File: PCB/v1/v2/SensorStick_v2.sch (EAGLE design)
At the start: 62 parts, among them IC1 STM32L412RBT6, J1 DST310S_32.768KHZ, J2 10118192-0001LF, U1 BMI088, U2 LD39050PU33R, Y1 8MHz

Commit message: Jesus - More merge changes
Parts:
- removed C2, C37: 4.7p, GQM2195C2E4R7BB12D(4_7p):GQM2195C2E4R7BB12D
- removed C3, C35: 20p, CC0402KPX7R7BB104(0402cap_foot):CC0402KPX7R7BB104
- removed J1: DST310S_32.768KHZ, ce-capstone-2022:DST310S_32.768KHZ_DST310S_32.768KHZ
- removed R4: 220, RC0805FR-10220RL:RC0805FR-10220RL
- removed Y1: 8MHz, ce-capstone:ABLS-8.000MHZ-B2-T
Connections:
- removed net N$3: C3.1, R4.2, Y1.1
- removed net PC14-OSC32-IN: C37.1, J1.1
- removed net PC15-OSC32-OUT: C2.1, J1.2
- removed net PH0-OSC-IN: C35.1, Y1.2
- removed net PH1-OSC-OUT: R4.1
- net GND: no longer C2.2, C3.2, C35.2, C37.2
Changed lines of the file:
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@@
 <part name="FB1" library="ce-capstone" deviceset="BK1608HS601-T" device=""/>
 <part name="GND4" library="supply1" library_urn="urn:adsk.eagle:library:371" deviceset="GND" device=""/>
-<part name="Y1" library="ce-capstone" deviceset="ABLS-8.000MHZ-B2-T" device="" value="8MHz"/>
-<part name="GND5" library="supply1" library_urn="urn:adsk.eagle:library:371" deviceset="GND" device=""/>
-<part name="GND6" library="supply1" library_urn="urn:adsk.eagle:library:371" deviceset="GND" device=""/>
 <part name="GND7" library="supply1" library_urn="urn:adsk.eagle:library:371" deviceset="GND" device=""/>
 <part name="J2" library="ce-capstone" deviceset="10118192-0001LF" device=""/>
@@
 <part name="C33" library="GRT31C5C2A104JA12L(0_1u)" deviceset="GRT31C5C2A104JA12L" device="" value="100n"/>
 <part name="C34" library="GRT31C5C2A104JA12L(0_1u)" deviceset="GRT31C5C2A104JA12L" device="" value="100n"/>
-<part name="C37" library="GQM2195C2E4R7BB12D(4_7p)" deviceset="GQM2195C2E4R7BB12D" device="" value="4.7p"/>
 <part name="C39" library="GRT21BC71H475KE13L(4_7u)" deviceset="GRT21BC71H475KE13L" device="" value="4.7u"/>
 <part name="C40" library="GRM31CR73A103KW03L(0_01u)" deviceset="GRM31CR73A103KW03L" device="" value="10n"/>
-<part name="C2" library="GQM2195C2E4R7BB12D(4_7p)" deviceset="GQM2195C2E4R7BB12D" device="" value="4.7p"/>
 <part name="C4" library="GRM219R61H105KA73D(1u)" deviceset="GRM219R61H105KA73D" device="" value="1u"/>
-<part name="R4" library="RC0805FR-10220RL" deviceset="RC0805FR-10220RL" device="" value="220"/>
 <part name="R6" library="RC0805FR-131KL" deviceset="RC0805FR-131KL" device="" value="1K"/>
 <part name="R7" library="RC0805FR-131KL" deviceset="RC0805FR-131KL" device="" value="1K"/>
@@
 <part name="JP3" library="pinhead" library_urn="urn:adsk.eagle:library:325" deviceset="PINHD-2X4" device="" package3d_urn="urn:adsk.eagle:package:22461/2"/>
 <part name="JP8" library="pinhead" library_urn="urn:adsk.eagle:library:325" deviceset="PINHD-2X4" device="" package3d_urn="urn:adsk.eagle:package:22461/2"/>
-<part name="J1" library="ce-capstone-2022" deviceset="DST310S_32.768KHZ_DST310S_32.768KHZ" device="" value="DST310S_32.768KHZ"/>
 <part name="S1" library="ce-capstone-2022" deviceset="SWITCH-TACT_DTSM-6" device=""/>
 <part name="D1" library="ce-capstone-2022" deviceset="1N5819HW-7-F_1N5819HW-7-F" device=""/>
-<part name="C35" library="CC0402KPX7R7BB104(0402cap_foot)" deviceset="CC0402KPX7R7BB104" device="" value="20p"/>
-<part name="C3" library="CC0402KPX7R7BB104(0402cap_foot)" deviceset="CC0402KPX7R7BB104" device="" value="20p"/>
 <part name="U1" library="BMI088" deviceset="BMI088" device=""/>
 <part name="FRAME2" library="frames" library_urn="urn:adsk.eagle:library:229" deviceset="FRAME_C_L" device=""/>
@@
 <attribute name="VALUE" x="-96.52" y="99.06" size="1.778" layer="96"/>
 </instance>
-<instance part="Y1" gate="G$1" x="7.62" y="208.28" smashed="yes" rot="R90">
-<attribute name="NAME" x="5.333490625" y="203.19886875" size="1.7784" layer="95" rot="R90"/>
-<attribute name="VALUE" x="11.43073125" y="202.69093125" size="1.778340625" layer="96" rot="R90"/>
-</instance>
-<instance part="GND5" gate="1" x="50.8" y="198.12" smashed="yes">
-<attribute name="VALUE" x="48.26" y="195.58" size="1.778" layer="96"/>
-</instance>
-<instance part="GND6" gate="1" x="50.8" y="167.64" smashed="yes">
-<attribute name="VALUE" x="48.26" y="165.1" size="1.778" layer="96"/>
-</instance>
 <instance part="GND7" gate="1" x="299.72" y="144.78" smashed="yes">
 <attribute name="VALUE" x="297.18" y="139.7" size="1.778" layer="96"/>
@@
 <attribute name="VALUE" x="-110.49" y="143.51" size="1.778" layer="96" align="center-left"/>
 </instance>
-<instance part="C37" gate="G$1" x="22.86" y="185.42" smashed="yes">
-<attribute name="NAME" x="31.75" y="191.77" size="1.778" layer="95" align="center-left"/>
-<attribute name="VALUE" x="31.75" y="189.23" size="1.778" layer="96" align="center-left"/>
-</instance>
 <instance part="C39" gate="G$1" x="-124.46" y="223.52" smashed="yes">
 <attribute name="NAME" x="-115.57" y="229.87" size="1.778" layer="95" align="center-left"/>
@@
 <attribute name="VALUE" x="-110.49" y="113.03" size="1.778" layer="96" align="center-left"/>
 </instance>
-<instance part="C2" gate="G$1" x="22.86" y="170.18" smashed="yes">
-<attribute name="NAME" x="31.75" y="176.53" size="1.778" layer="95" align="center-left"/>
-<attribute name="VALUE" x="31.75" y="173.99" size="1.778" layer="96" align="center-left"/>
-</instance>
 <instance part="C4" gate="G$1" x="271.78" y="223.52" smashed="yes" rot="R90">
 <attribute name="NAME" x="265.43" y="232.41" size="1.778" layer="95" rot="R90" align="center-left"/>
 <attribute name="VALUE" x="267.97" y="232.41" size="1.778" layer="96" rot="R90" align="center-left"/>
 </instance>
-<instance part="R4" gate="G$1" x="-30.48" y="200.66" smashed="yes">
-<attribute name="NAME" x="-16.51" y="207.01" size="1.778" layer="95" align="center-left"/>
-<attribute name="VALUE" x="-16.51" y="204.47" size="1.778" layer="96" align="center-left"/>
-</instance>
 <instance part="R6" gate="G$1" x="299.72" y="218.44" smashed="yes" rot="R90">
 <attribute name="NAME" x="293.37" y="232.41" size="1.778" layer="95" rot="R90" align="center-left"/>
@@
 <attribute name="VALUE" x="-133.35" y="45.72" size="1.778" layer="96"/>
 </instance>
-<instance part="J1" gate="G$1" x="-2.54" y="177.8" smashed="yes">
-<attribute name="NAME" x="13.97" y="180.34" size="1.778" layer="95" align="center-left"/>
-<attribute name="VALUE" x="1.27" y="182.88" size="1.778" layer="96" align="center-left"/>
-</instance>
 <instance part="S1" gate="G$1" x="302.26" y="167.64" smashed="yes" rot="R180">
 <attribute name="NAME" x="308.61" y="170.18" size="1.778" layer="95" rot="R270"/>
@@
 <attribute name="NAME" x="173.99" y="231.14" size="1.778" layer="95" rot="R180" align="center-left"/>
 <attribute name="VALUE" x="189.23" y="241.3" size="1.778" layer="96" rot="R180" align="center-left"/>
-</instance>
-<instance part="C35" gate="G$1" x="25.4" y="215.9" smashed="yes">
-<attribute name="NAME" x="31.75" y="224.79" size="1.778" layer="95" align="center-left"/>
-<attribute name="VALUE" x="31.75" y="222.25" size="1.778" layer="96" align="center-left"/>
-</instance>
-<instance part="C3" gate="G$1" x="25.4" y="200.66" smashed="yes">
-<attribute name="NAME" x="34.29" y="207.01" size="1.778" layer="95" align="center-left"/>
-<attribute name="VALUE" x="34.29" y="204.47" size="1.778" layer="96" align="center-left"/>
 </instance>
 <instance part="U1" gate="A" x="-30.48" y="96.52" smashed="yes">
@@
 </segment>
 <segment>
-<pinref part="GND5" gate="1" pin="GND"/>
-<wire x1="50.8" y1="215.9" x2="50.8" y2="200.66" width="0.1524" layer="91"/>
-<wire x1="38.1" y1="200.66" x2="50.8" y2="200.66" width="0.1524" layer="91"/>
-<junction x="50.8" y="200.66"/>
-<wire x1="38.1" y1="215.9" x2="50.8" y2="215.9" width="0.1524" layer="91"/>
-<pinref part="C35" gate="G$1" pin="2"/>
-<pinref part="C3" gate="G$1" pin="2"/>
-</segment>
-<segment>
-<pinref part="GND6" gate="1" pin="GND"/>
-<wire x1="50.8" y1="185.42" x2="50.8" y2="170.18" width="0.1524" layer="91"/>
-<pinref part="C2" gate="G$1" pin="2"/>
-<wire x1="35.56" y1="170.18" x2="50.8" y2="170.18" width="0.1524" layer="91"/>
-<junction x="50.8" y="170.18"/>
-<pinref part="C37" gate="G$1" pin="2"/>
-<wire x1="35.56" y1="185.42" x2="50.8" y2="185.42" width="0.1524" layer="91"/>
-</segment>
-<segment>
 <wire x1="276.86" y1="157.48" x2="299.72" y2="157.48" width="0.1524" layer="91"/>
 <wire x1="299.72" y1="157.48" x2="302.26" y2="157.48" width="0.1524" layer="91"/>
@@
 </segment>
 </net>
-<net name="PH1-OSC-OUT" class="0">
-<segment>
-<wire x1="-30.48" y1="200.66" x2="-50.8" y2="200.66" width="0.1524" layer="91"/>
-<label x="-45.72" y="200.66" size="1.778" layer="95"/>
-<pinref part="R4" gate="G$1" pin="1"/>
-</segment>
-</net>
-<net name="PH0-OSC-IN" class="0">
-<segment>
-<pinref part="Y1" gate="G$1" pin="2"/>
-<wire x1="7.62" y1="213.36" x2="7.62" y2="215.9" width="0.1524" layer="91"/>
-<wire x1="7.62" y1="215.9" x2="-40.64" y2="215.9" width="0.1524" layer="91"/>
-<label x="-40.64" y="215.9" size="1.778" layer="95"/>
-<wire x1="7.62" y1="215.9" x2="25.4" y2="215.9" width="0.1524" layer="91"/>
-<junction x="7.62" y="215.9"/>
-<pinref part="C35" gate="G$1" pin="1"/>
-</segment>
-</net>
-<net name="PC15-OSC32-OUT" class="0">
-<segment>
-<wire x1="22.86" y1="170.18" x2="-2.54" y2="170.18" width="0.1524" layer="91"/>
-<label x="-45.72" y="170.18" size="1.778" layer="95"/>
-<pinref part="C2" gate="G$1" pin="1"/>
-<pinref part="J1" gate="G$1" pin="2"/>
-<wire x1="-2.54" y1="170.18" x2="-48.26" y2="170.18" width="0.1524" layer="91"/>
-<wire x1="-2.54" y1="175.26" x2="-2.54" y2="170.18" width="0.1524" layer="91"/>
-<junction x="-2.54" y="170.18"/>
-</segment>
-</net>
-<net name="PC14-OSC32-IN" class="0">
-<segment>
-<wire x1="22.86" y1="185.42" x2="-2.54" y2="185.42" width="0.1524" layer="91"/>
-<label x="-45.72" y="185.42" size="1.778" layer="95"/>
-<pinref part="C37" gate="G$1" pin="1"/>
-<pinref part="J1" gate="G$1" pin="1"/>
-<wire x1="-2.54" y1="185.42" x2="-48.26" y2="185.42" width="0.1524" layer="91"/>
-<wire x1="-2.54" y1="177.8" x2="-2.54" y2="185.42" width="0.1524" layer="91"/>
-<junction x="-2.54" y="185.42"/>
-</segment>
-</net>
 <net name="5V_IN" class="0">
 <segment>
@@
 </segment>
 </net>
-<net name="N$3" class="0">
-<segment>
-<pinref part="Y1" gate="G$1" pin="1"/>
-<wire x1="-12.7" y1="200.66" x2="7.62" y2="200.66" width="0.1524" layer="91"/>
-<wire x1="7.62" y1="203.2" x2="7.62" y2="200.66" width="0.1524" layer="91"/>
-<wire x1="7.62" y1="200.66" x2="25.4" y2="200.66" width="0.1524" layer="91"/>
-<junction x="7.62" y="200.66"/>
-<pinref part="R4" gate="G$1" pin="2"/>
-<pinref part="C3" gate="G$1" pin="1"/>
-</segment>
-</net>

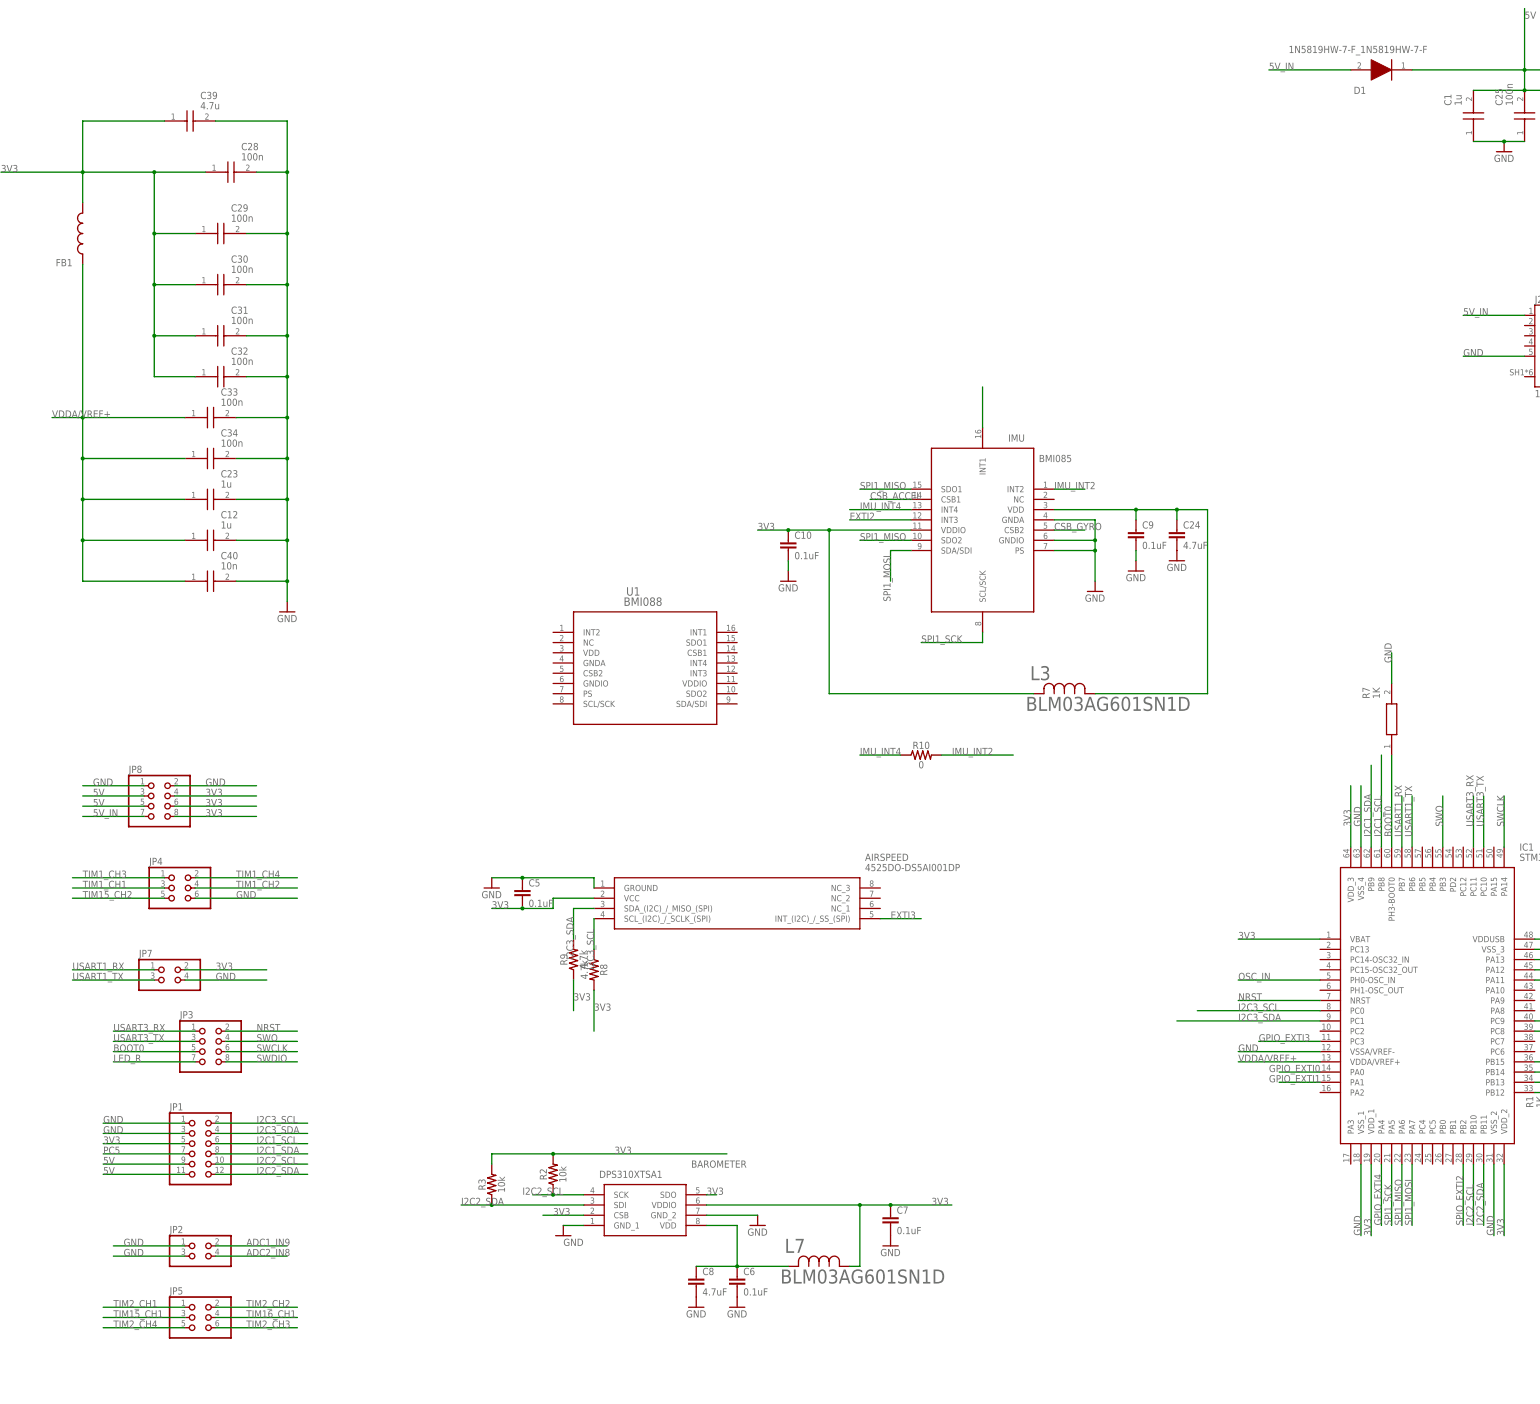
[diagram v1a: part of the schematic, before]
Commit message: Jesus - Schematic should be complete
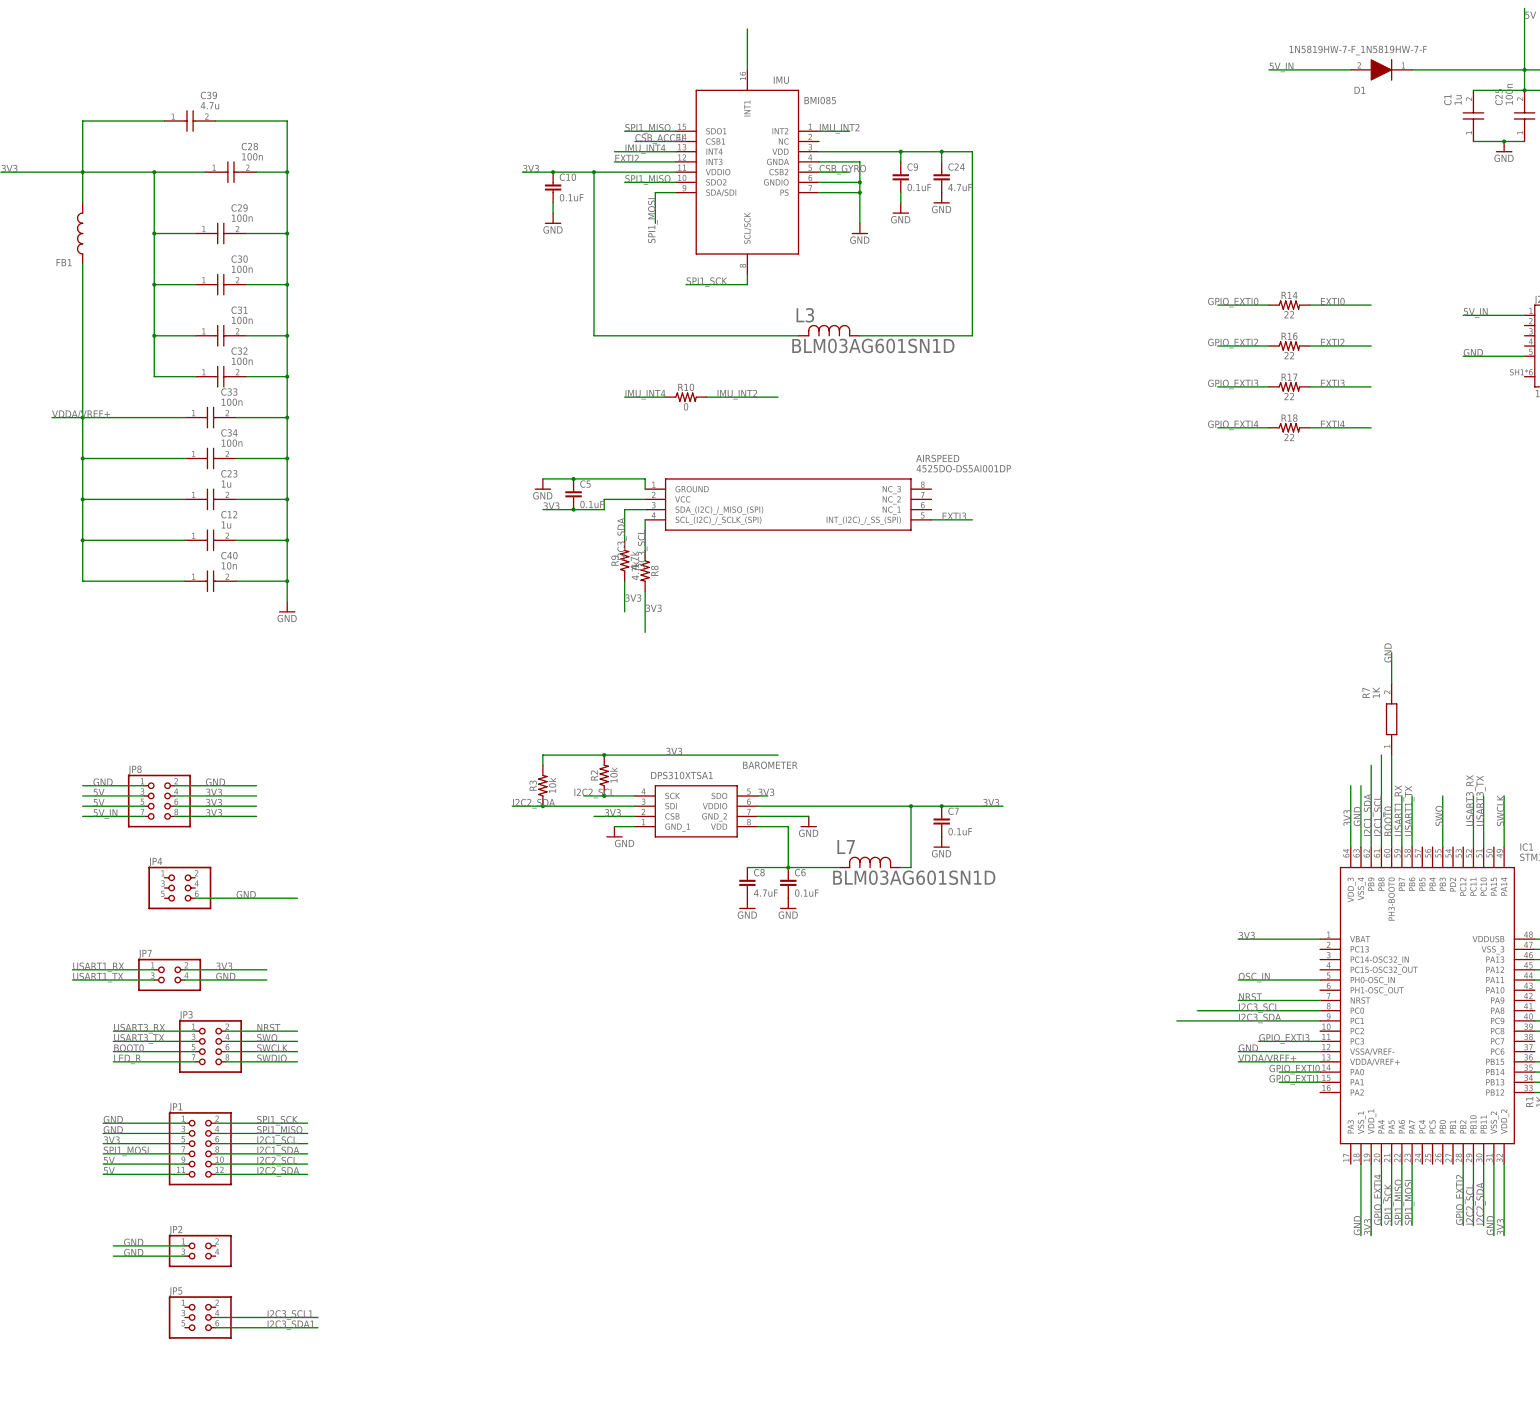
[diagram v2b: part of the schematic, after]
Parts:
- removed U1: BMI088, BMI088:BMI088
- added R14, R16, R17, R18: 22, SparkFun-Resistors:22OHM-0402-1/10W-1%
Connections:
- net TIM16_CH1 renamed I2C3_SCL1
- net TIM2_CH3 renamed I2C3_SDA1
- removed net ADC1_IN9: JP2.2
- removed net ADC2_IN8: JP2.4
- removed net PC5: JP1.7
- removed net SPIO_EXTI2: IC1.PB2
- removed net TIM15_CH1: JP5.3
- removed net TIM15_CH2: JP4.5
- removed net TIM1_CH1: JP4.3
- removed net TIM1_CH2: JP4.4
- removed net TIM1_CH3: JP4.1
- removed net TIM1_CH4: JP4.2
- removed net TIM2_CH1: JP5.1
- removed net TIM2_CH2: JP5.2
- removed net TIM2_CH4: JP5.5
- new net EXTI4: R18.2
- new net GPIO_EXTI2: IC1.PB2, R16.1
- net EXTI0: now also R14.2
- net EXTI2: now also R16.2
- net EXTI3: now also R17.2
- net GPIO_EXTI0: now also R14.1
- net GPIO_EXTI3: now also R17.1
- net GPIO_EXTI4: now also R18.1
- net I2C3_SCL: no longer JP1.2
- net I2C3_SDA: no longer JP1.4
- net SPI1_MISO: now also JP1.4
- net SPI1_MOSI: now also JP1.7
- net SPI1_SCK: now also JP1.2
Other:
- moved on the sheet: AIRSPEED, BAROMETER, C10, C24, C5, C6, C7, C8, C9, IMU, L3, L7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
